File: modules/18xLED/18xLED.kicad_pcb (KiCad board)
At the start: 2 copper layers, 40.6 x 40.6 mm, 44 parts, among them J1 Conn_01x10_Male, J2 Conn_01x10_Male

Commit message: LEDs. Add photomask in pdf.
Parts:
- moved D1 15.1 mm to (100.6, 65.4)
- moved D13 15.1 mm to (110.1, 52.7)
- moved D15 15.1 mm to (110.1, 57.8)
- moved D16 15.1 mm to (110.1, 60.3)
- moved D18 15.1 mm to (110.2, 65.4)
- moved D19 15.1 mm to (110.2, 67.9)
- moved D3 15.1 mm to (100.6, 60.3)
- moved D4 15.1 mm to (100.6, 57.8)
- moved D7 15.1 mm to (100.6, 52.7)
- moved R1 15.1 mm to (95.2, 65.4)
- moved R13 15.1 mm to (115.6, 52.7)
- moved R15 15.1 mm to (115.6, 57.8)
- moved R16 15.1 mm to (115.6, 60.3)
- moved R18 15.1 mm to (115.6, 65.4)
- moved R19 15.1 mm to (115.6, 67.9)
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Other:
- board text added: "06eece"
- board text removed: "hash"

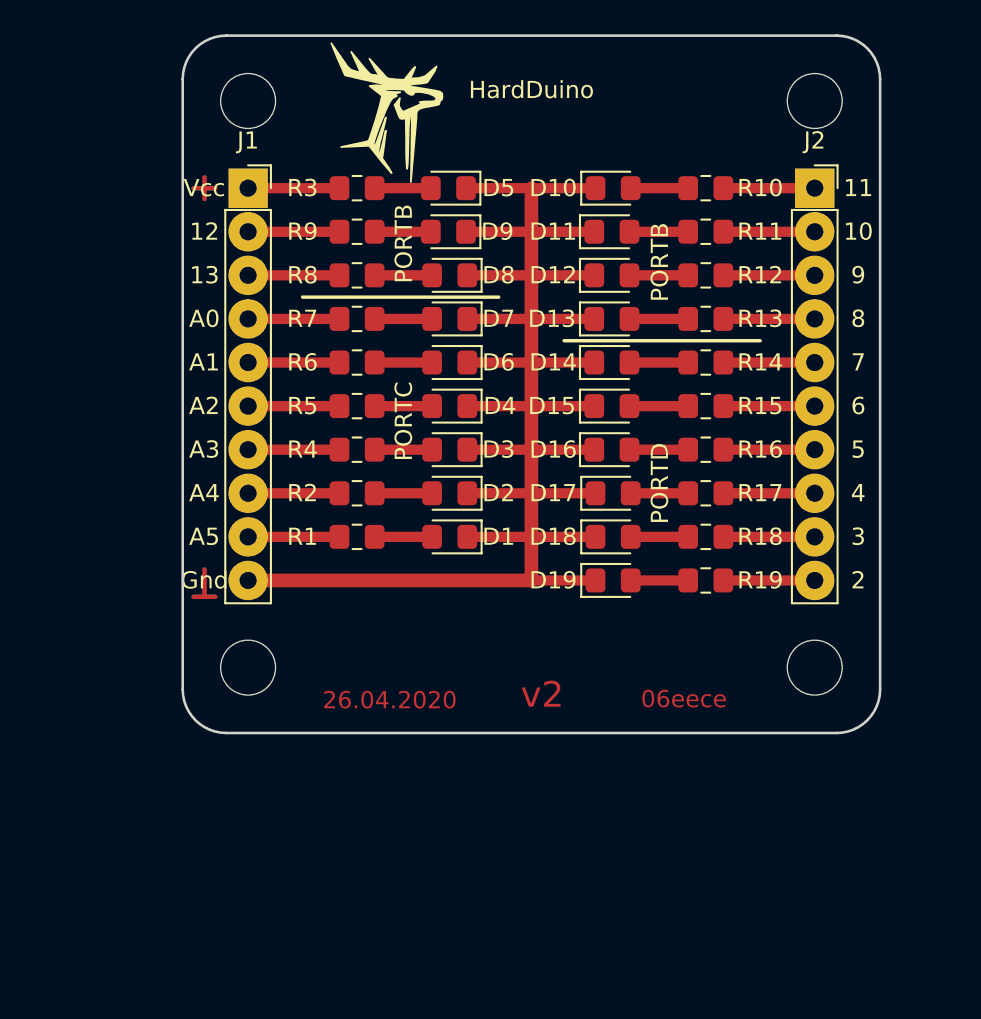
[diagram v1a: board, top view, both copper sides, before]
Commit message: 1x PCBs. Move holes to edges. Caution! This changes is uncompatible with previous versions...
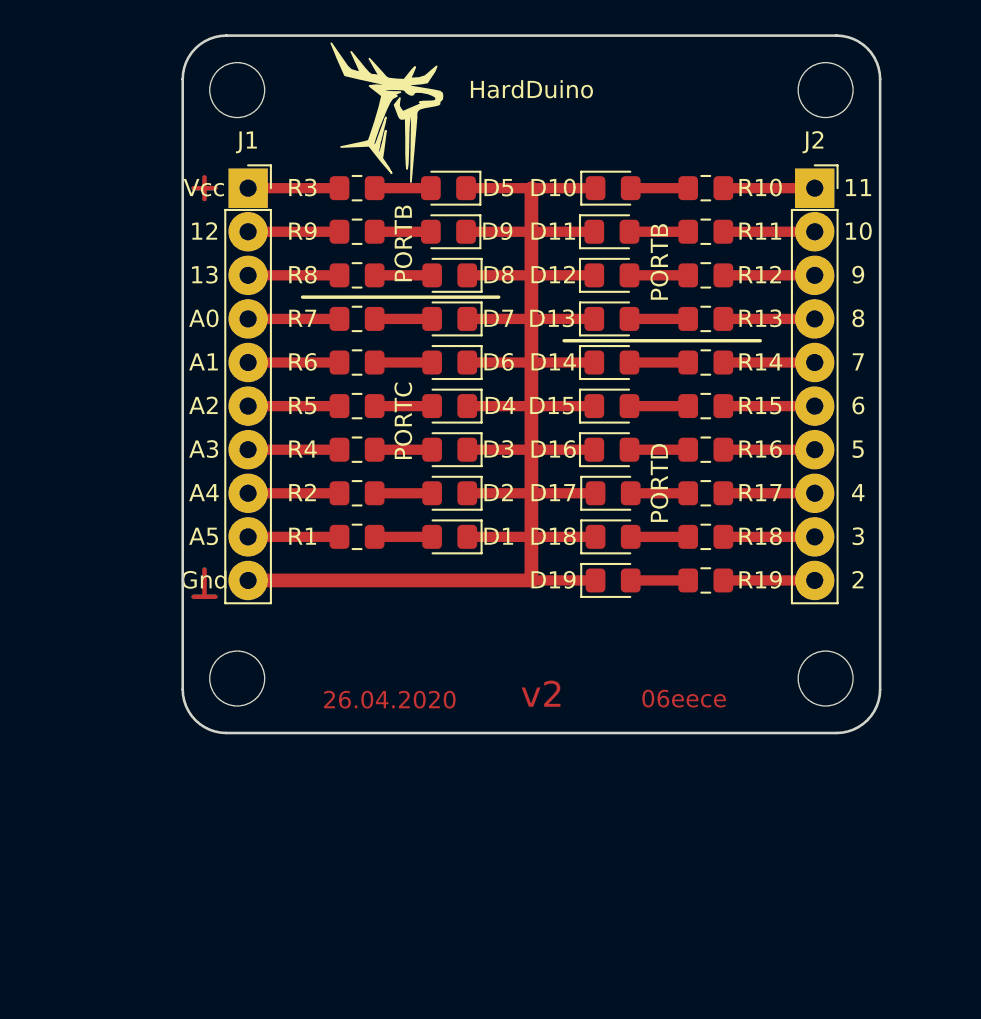
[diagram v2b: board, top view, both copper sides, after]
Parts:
- moved H1 0.90 mm to (88.3, 39.4)
- moved H3 0.90 mm to (122.6, 39.4)
- moved H2 0.90 mm to (88.3, 73.7)
- moved H4 0.90 mm to (122.6, 73.7)
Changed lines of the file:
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@@
   )
   (module MountingHole:MountingHole_3.2mm_M3 (layer F.Cu)
-    (at 88.9 40.005)
+    (at 88.2650 39.3700)
     (descr "Mounting Hole 3.2mm, no annular, M3")
     (tags "mounting hole 3.2mm no annular m3")
@@
   )
   (module MountingHole:MountingHole_3.2mm_M3 (layer F.Cu)
-    (at 88.9 73.025)
+    (at 88.2650 73.6600)
     (descr "Mounting Hole 3.2mm, no annular, M3")
     (tags "mounting hole 3.2mm no annular m3")
@@
   )
   (module MountingHole:MountingHole_3.2mm_M3 (layer F.Cu)
-    (at 121.92 40.005)
+    (at 122.5550 39.3700)
     (descr "Mounting Hole 3.2mm, no annular, M3")
     (tags "mounting hole 3.2mm no annular m3")
@@
   )
   (module MountingHole:MountingHole_3.2mm_M3 (layer F.Cu)
-    (at 121.92 73.025)
+    (at 122.5550 73.6600)
     (descr "Mounting Hole 3.2mm, no annular, M3")
     (tags "mounting hole 3.2mm no annular m3")

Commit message: Fix hash & version
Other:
- board text added: "21.02.2021"
- board text added: "b4d799"
- board text added: "v2.3"
- board text removed: "06eece"
- board text removed: "26.04.2020"
- board text removed: "v2"

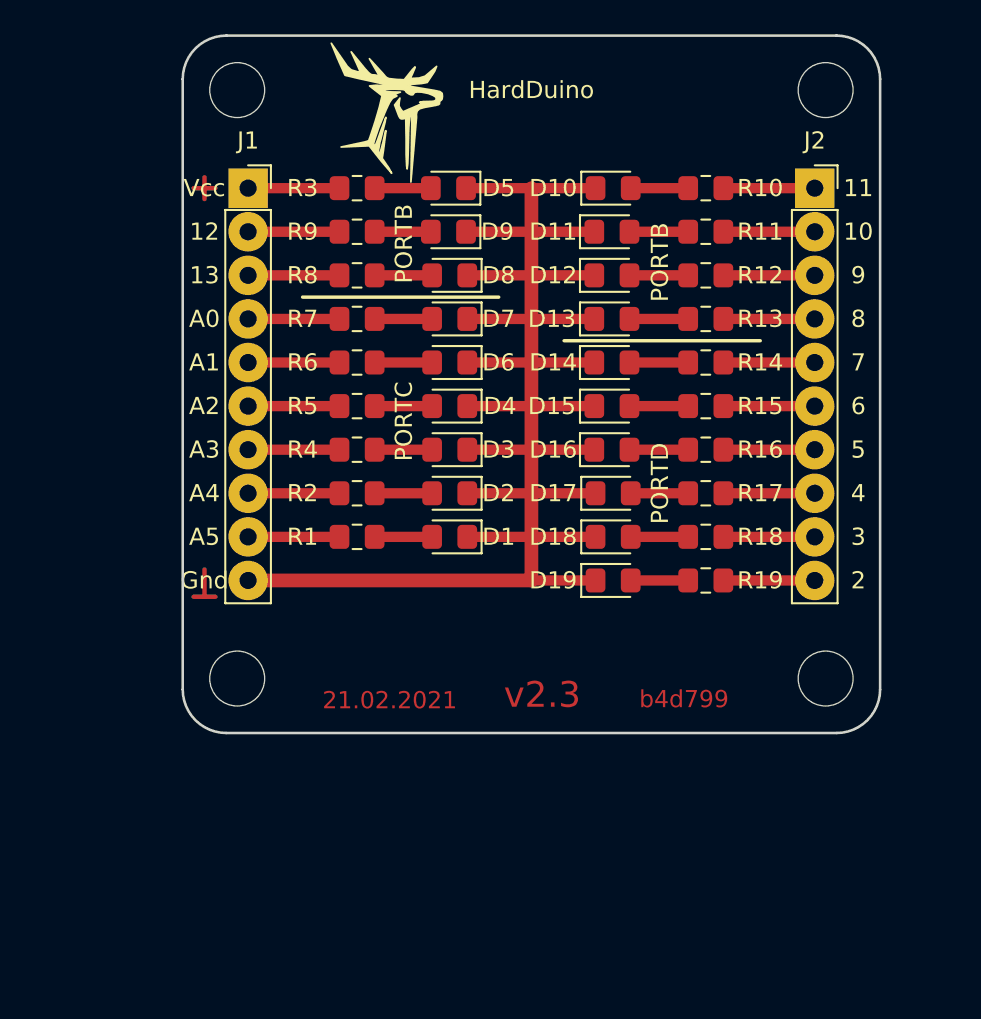
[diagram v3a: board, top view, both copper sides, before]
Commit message: Move mounting holes closer
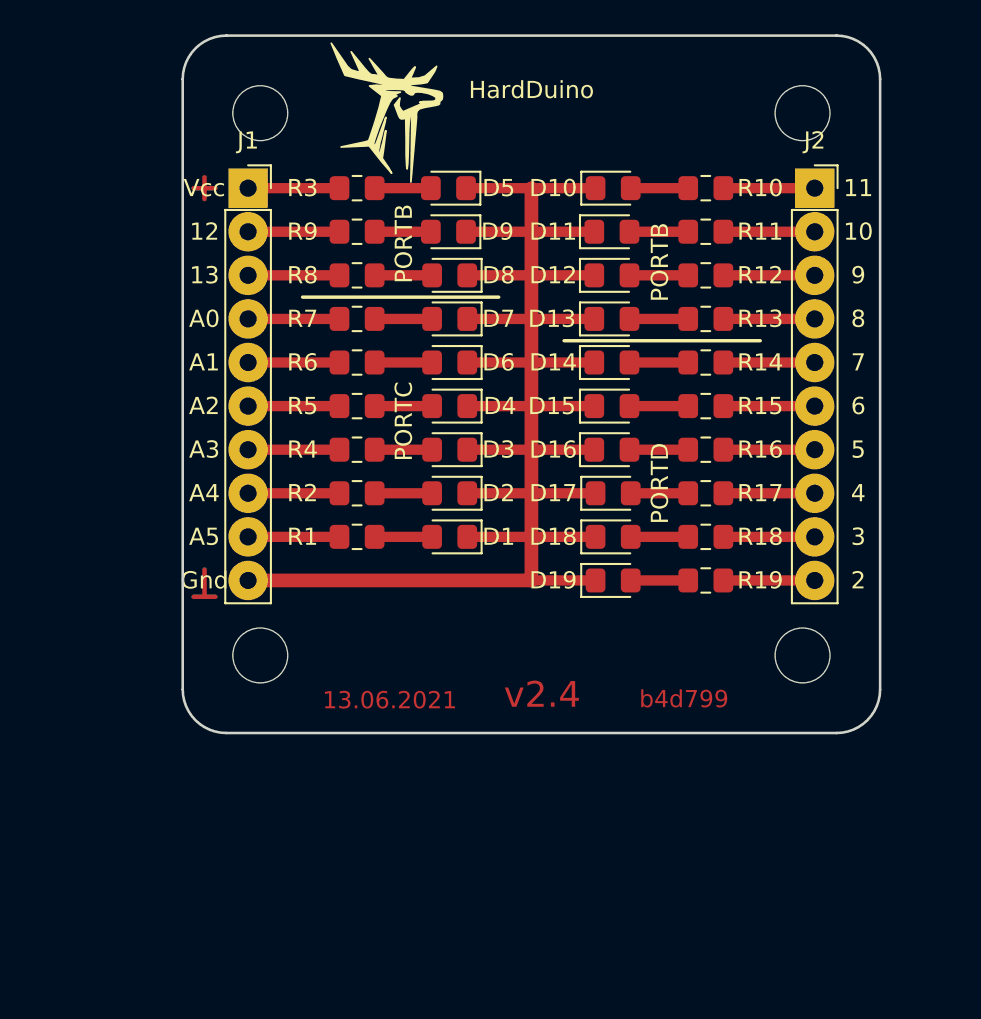
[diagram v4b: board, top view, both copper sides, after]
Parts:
- moved H3 1.90 mm to (121.2, 40.7)
- moved H4 1.90 mm to (121.2, 72.3)
- moved H1 1.90 mm to (89.6, 40.7)
- moved H2 1.90 mm to (89.6, 72.3)
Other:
- board text added: "13.06.2021"
- board text added: "v2.4"
- board text removed: "21.02.2021"
- board text removed: "v2.3"

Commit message: v2.5, size was changed to 31.1 x 31.92
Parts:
- moved H1 0.30 mm to (89.9, 40.6)
- moved H3 0.30 mm to (121.0, 40.6)
- moved H2 0.30 mm to (89.9, 72.5)
- moved H4 0.30 mm to (121.0, 72.5)
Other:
- board text added: "17.06.2021"
- board text added: "v2.5"
- board text removed: "13.06.2021"
- board text removed: "v2.4"

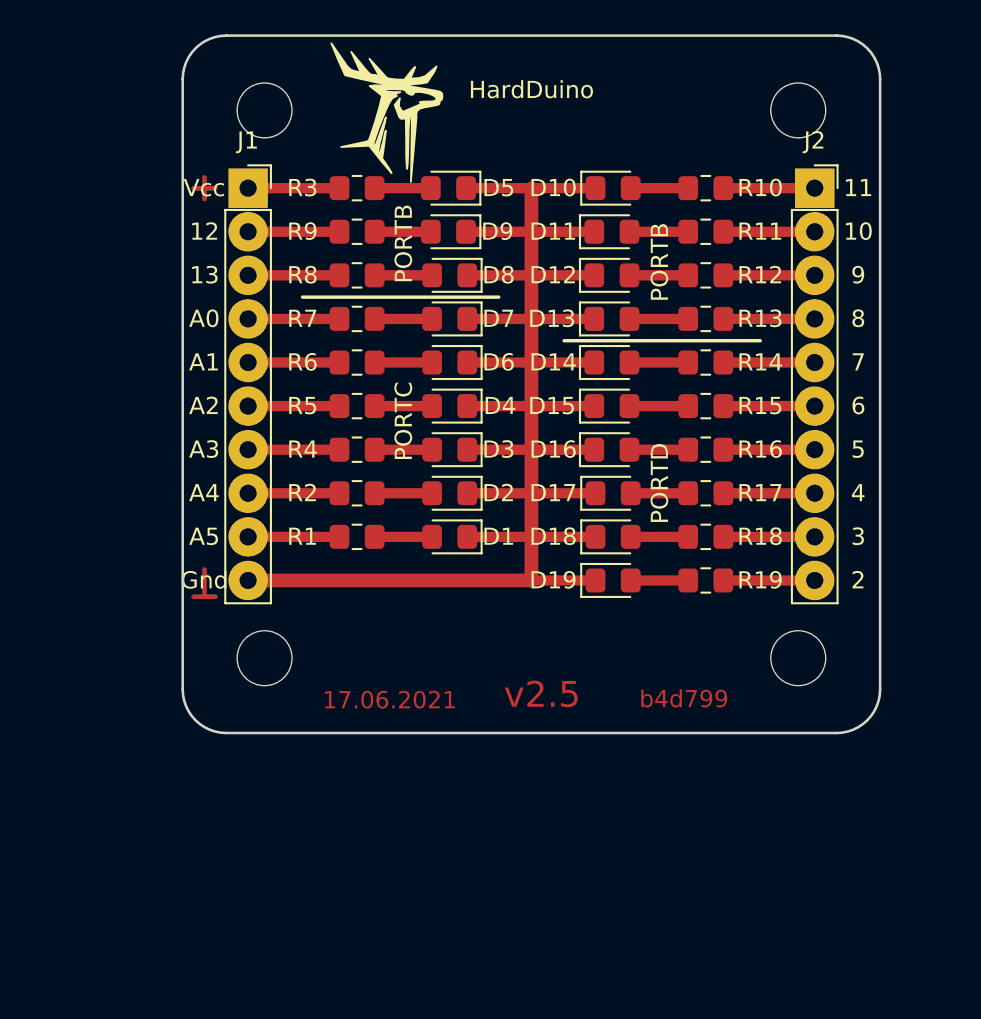
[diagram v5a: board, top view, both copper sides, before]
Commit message: All 1x shields was rotated clockwise
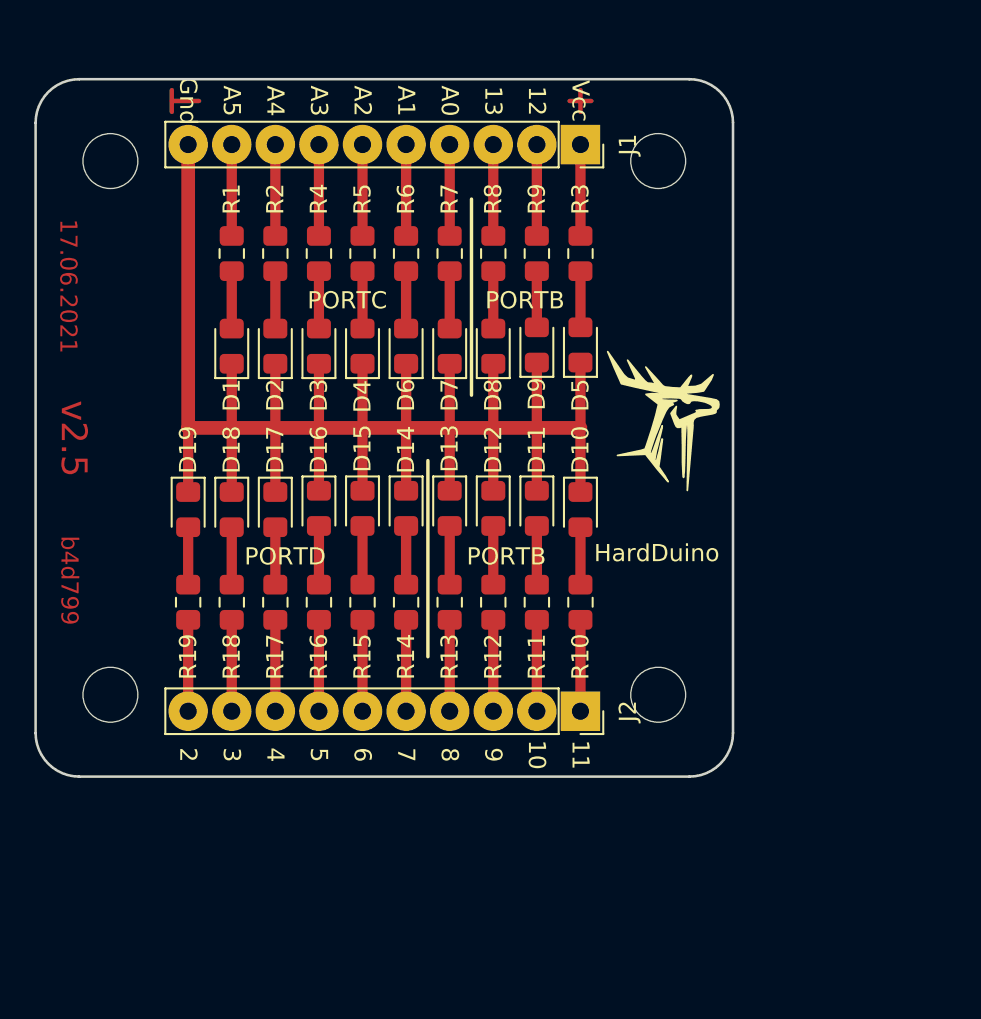
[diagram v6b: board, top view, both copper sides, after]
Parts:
- moved H4 40.1 mm to (80.9, 74.6), turned to 270 degrees
- moved H3 35.0 mm to (112.8, 74.6), turned to 270 degrees
- moved J2 33.4 mm to (108.3, 75.6), turned to 270 degrees
- moved H2 30.3 mm to (80.9, 43.5), turned to 270 degrees
- moved R19 30.2 mm to (85.4, 69.2), turned to 90 degrees
- moved R18 27.9 mm to (87.9, 69.2), turned to 90 degrees
- moved R17 25.9 mm to (90.5, 69.2), turned to 90 degrees
- moved R10 25.2 mm to (108.3, 69.2), turned to 90 degrees
- moved D19 25.1 mm to (85.4, 63.8), turned to 270 degrees
- moved R16 24.2 mm to (93.0, 69.2), turned to 90 degrees
- moved R11 23.7 mm to (105.7, 69.2), turned to 90 degrees
- moved H1 23.1 mm to (112.8, 43.5), turned to 270 degrees
- moved R15 23.0 mm to (95.6, 69.2), turned to 90 degrees
- moved R12 22.7 mm to (103.2, 69.2), turned to 90 degrees
- moved R14 22.4 mm to (98.1, 69.2), turned to 90 degrees
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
